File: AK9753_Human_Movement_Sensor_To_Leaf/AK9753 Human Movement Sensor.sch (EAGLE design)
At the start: 9 parts, among them J3 PTH, U2 AK9753

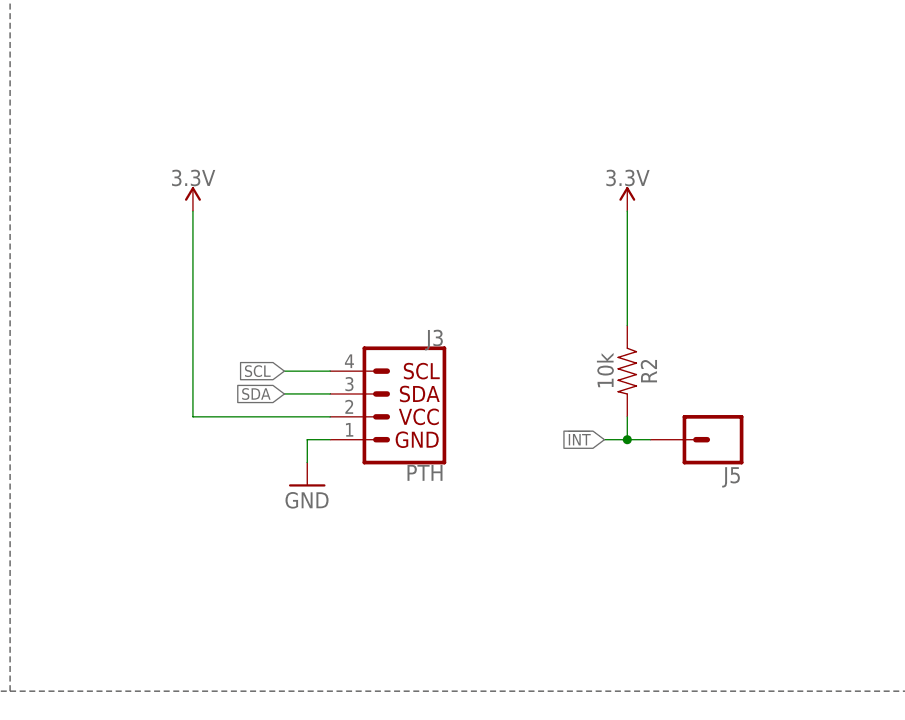
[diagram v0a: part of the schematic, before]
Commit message: Finished schematic
drawing board next
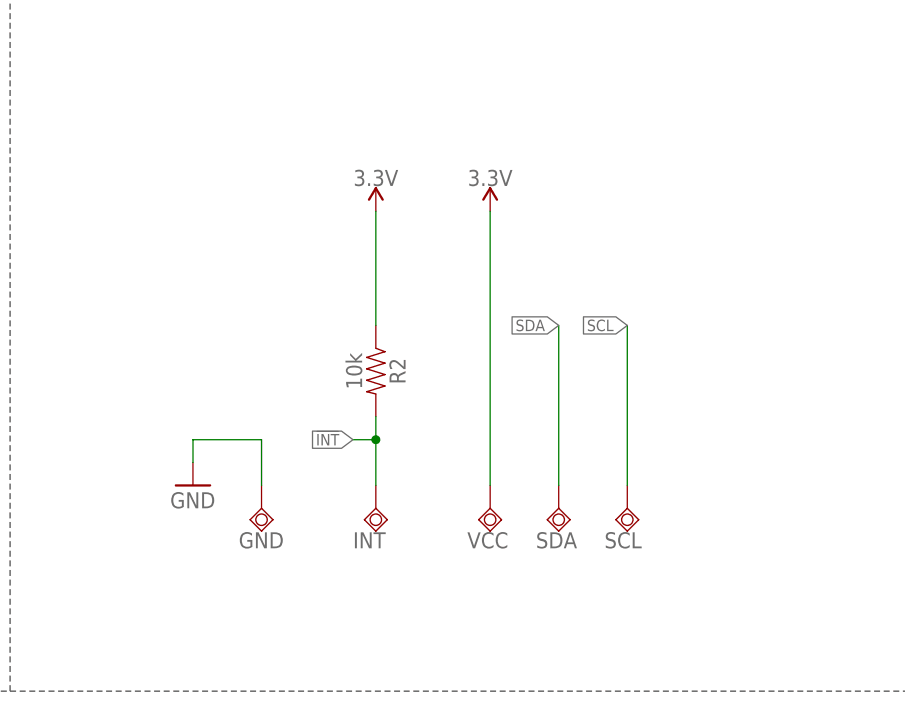
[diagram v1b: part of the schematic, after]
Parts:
- removed J3: PTH, SparkFun-Connectors:I2C_STANDARD_NO_SILK
- removed J5: (no value), SparkFun-Connectors:CONN_01PTH_NO_SILK_YES_STOP
- added GND, INT, SCL, SDA, VCC: TPSQTP20R, testpad:TPSQTP20R
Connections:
- net !INT: now also INT.TP; no longer J5.1
- net 3.3V: now also VCC.TP; no longer J3.2
- net GND: now also GND.TP; no longer J3.1
- net SCL: now also SCL.TP; no longer J3.4
- net SDA: now also SDA.TP; no longer J3.3
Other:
- moved on the sheet: R2
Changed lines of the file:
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@@
 <part name="GND4" library="SparkFun" deviceset="GND" device=""/>
 <part name="SUPPLY7" library="SparkFun-PowerSymbols" deviceset="3.3V" device=""/>
-<part name="J3" library="SparkFun-Connectors" deviceset="I2C_STANDARD" device="_NO_SILK" value="PTH"/>
 <part name="GND7" library="SparkFun" deviceset="GND" device=""/>
 <part name="C4" library="SparkFun-Capacitors" deviceset="1.0UF" device="-0603-16V-10%" value="1.0uF"/>
-<part name="J5" library="SparkFun-Connectors" deviceset="CONN_01" device="PTH_NO_SILK_YES_STOP"/>
 <part name="U2" library="SparkFun-Sensors" deviceset="AK9750" device="&quot;" value="AK9753"/>
 <part name="SUPPLY6" library="SparkFun-PowerSymbols" deviceset="3.3V" device=""/>
@@
 <part name="R6" library="SparkFun-Resistors" deviceset="330OHM" device="-0603-1/10W-1%" value="330"/>
 <part name="SUPPLY10" library="SparkFun-PowerSymbols" deviceset="3.3V" device=""/>
+<part name="SDA" library="testpad" library_urn="urn:adsk.eagle:library:385" deviceset="TPSQ" device="TP20R" package3d_urn="urn:adsk.eagle:package:27973/1"/>
+<part name="VCC" library="testpad" library_urn="urn:adsk.eagle:library:385" deviceset="TPSQ" device="TP20R" package3d_urn="urn:adsk.eagle:package:27973/1"/>
+<part name="SCL" library="testpad" library_urn="urn:adsk.eagle:library:385" deviceset="TPSQ" device="TP20R" package3d_urn="urn:adsk.eagle:package:27973/1"/>
+<part name="GND" library="testpad" library_urn="urn:adsk.eagle:library:385" deviceset="TPSQ" device="TP20R" package3d_urn="urn:adsk.eagle:package:27973/1"/>
+<part name="INT" library="testpad" library_urn="urn:adsk.eagle:library:385" deviceset="TPSQ" device="TP20R" package3d_urn="urn:adsk.eagle:package:27973/1"/>
 </parts>
 <sheets>
@@
 <attribute name="VALUE" x="60.96" y="101.6" size="1.778" layer="96"/>
 </instance>
-<instance part="SUPPLY7" gate="G$1" x="160.02" y="144.78" smashed="yes">
-<attribute name="VALUE" x="160.02" y="147.574" size="1.778" layer="96" align="bottom-center"/>
-</instance>
-<instance part="J3" gate="G$1" x="182.88" y="121.92" smashed="yes" rot="MR0">
-<attribute name="VALUE" x="187.96" y="116.586" size="1.778" layer="96" font="vector" rot="MR0" align="top-left"/>
-<attribute name="NAME" x="187.96" y="129.794" size="1.778" layer="95" font="vector" rot="MR0"/>
-</instance>
-<instance part="GND7" gate="1" x="172.72" y="114.3" smashed="yes">
-<attribute name="VALUE" x="170.18" y="111.76" size="1.778" layer="96"/>
+<instance part="SUPPLY7" gate="G$1" x="193.04" y="144.78" smashed="yes">
+<attribute name="VALUE" x="193.04" y="147.574" size="1.778" layer="96" align="bottom-center"/>
+</instance>
+<instance part="GND7" gate="1" x="160.02" y="114.3" smashed="yes">
+<attribute name="VALUE" x="157.48" y="111.76" size="1.778" layer="96"/>
 </instance>
 <instance part="C4" gate="G$1" x="63.5" y="114.3" smashed="yes">
@@
 <attribute name="VALUE" x="65.024" y="112.141" size="1.778" layer="96" font="vector"/>
 </instance>
-<instance part="J5" gate="G$1" x="218.44" y="119.38" smashed="yes" rot="R180">
-<attribute name="VALUE" x="220.98" y="124.206" size="1.778" layer="96" font="vector" rot="R180"/>
-<attribute name="NAME" x="220.98" y="116.332" size="1.778" layer="95" font="vector" rot="R180"/>
-</instance>
 <instance part="U2" gate="U1" x="88.9" y="116.84" smashed="yes">
 <attribute name="NAME" x="78.74" y="125.222" size="1.778" layer="95" font="vector"/>
@@
 <attribute name="VALUE" x="52.324" y="112.141" size="1.778" layer="96" font="vector"/>
 </instance>
-<instance part="R2" gate="G$1" x="208.28" y="127" smashed="yes" rot="R270">
-<attribute name="NAME" x="209.804" y="127" size="1.778" layer="95" font="vector" rot="R270" align="bottom-center"/>
-<attribute name="VALUE" x="206.756" y="127" size="1.778" layer="96" font="vector" rot="R270" align="top-center"/>
-</instance>
-<instance part="SUPPLY9" gate="G$1" x="208.28" y="144.78" smashed="yes">
-<attribute name="VALUE" x="208.28" y="147.574" size="1.778" layer="96" align="bottom-center"/>
+<instance part="R2" gate="G$1" x="180.34" y="127" smashed="yes" rot="R270">
+<attribute name="NAME" x="181.864" y="127" size="1.778" layer="95" font="vector" rot="R270" align="bottom-center"/>
+<attribute name="VALUE" x="178.816" y="127" size="1.778" layer="96" font="vector" rot="R270" align="top-center"/>
+</instance>
+<instance part="SUPPLY9" gate="G$1" x="180.34" y="144.78" smashed="yes">
+<attribute name="VALUE" x="180.34" y="147.574" size="1.778" layer="96" align="bottom-center"/>
 </instance>
 <instance part="R6" gate="G$1" x="63.5" y="132.08" smashed="yes" rot="R90">
@@
 <instance part="SUPPLY10" gate="G$1" x="63.5" y="139.7" smashed="yes">
 <attribute name="VALUE" x="63.5" y="142.494" size="1.778" layer="96" align="bottom-center"/>
+</instance>
+<instance part="SDA" gate="G$1" x="200.66" y="111.76" smashed="yes">
+<attribute name="NAME" x="198.12" y="107.315" size="1.778" layer="95"/>
+<attribute name="TP_SIGNAL_NAME" x="203.2" y="110.49" size="1.778" layer="97"/>
+</instance>
+<instance part="VCC" gate="G$1" x="193.04" y="111.76" smashed="yes">
+<attribute name="NAME" x="190.5" y="107.315" size="1.778" layer="95"/>
+<attribute name="TP_SIGNAL_NAME" x="195.58" y="110.49" size="1.778" layer="97"/>
+</instance>
+<instance part="SCL" gate="G$1" x="208.28" y="111.76" smashed="yes">
+<attribute name="NAME" x="205.74" y="107.315" size="1.778" layer="95"/>
+<attribute name="TP_SIGNAL_NAME" x="210.82" y="110.49" size="1.778" layer="97"/>
+</instance>
+<instance part="GND" gate="G$1" x="167.64" y="111.76" smashed="yes">
+<attribute name="NAME" x="165.1" y="107.315" size="1.778" layer="95"/>
+<attribute name="TP_SIGNAL_NAME" x="170.18" y="110.49" size="1.778" layer="97"/>
+</instance>
+<instance part="INT" gate="G$1" x="180.34" y="111.76" smashed="yes">
+<attribute name="NAME" x="177.8" y="107.315" size="1.778" layer="95"/>
+<attribute name="TP_SIGNAL_NAME" x="182.88" y="110.49" size="1.778" layer="97"/>
 </instance>
 </instances>
@@
 </segment>
 <segment>
-<pinref part="J3" gate="G$1" pin="2"/>
-<wire x1="175.26" y1="121.92" x2="160.02" y2="121.92" width="0.1524" layer="91"/>
-<wire x1="160.02" y1="121.92" x2="160.02" y2="144.78" width="0.1524" layer="91"/>
+<wire x1="193.04" y1="114.3" x2="193.04" y2="144.78" width="0.1524" layer="91"/>
 <pinref part="SUPPLY7" gate="G$1" pin="3.3V"/>
+<pinref part="VCC" gate="G$1" pin="TP"/>
 </segment>
 <segment>
@@
 <pinref part="SUPPLY9" gate="G$1" pin="3.3V"/>
 <pinref part="R2" gate="G$1" pin="1"/>
-<wire x1="208.28" y1="132.08" x2="208.28" y2="144.78" width="0.1524" layer="91"/>
+<wire x1="180.34" y1="132.08" x2="180.34" y2="144.78" width="0.1524" layer="91"/>
 </segment>
 <segment>
@@
 </segment>
 <segment>
-<pinref part="J3" gate="G$1" pin="1"/>
-<wire x1="175.26" y1="119.38" x2="172.72" y2="119.38" width="0.1524" layer="91"/>
-<wire x1="172.72" y1="119.38" x2="172.72" y2="116.84" width="0.1524" layer="91"/>
+<wire x1="160.02" y1="119.38" x2="160.02" y2="116.84" width="0.1524" layer="91"/>
 <pinref part="GND7" gate="1" pin="GND"/>
+<pinref part="GND" gate="G$1" pin="TP"/>
+<wire x1="160.02" y1="119.38" x2="167.64" y2="119.38" width="0.1524" layer="91"/>
+<wire x1="167.64" y1="119.38" x2="167.64" y2="114.3" width="0.1524" layer="91"/>
 </segment>
 <segment>
@@
 </segment>
 <segment>
-<pinref part="J3" gate="G$1" pin="4"/>
-<wire x1="175.26" y1="127" x2="170.18" y2="127" width="0.1524" layer="91"/>
-<label x="170.18" y="127" size="1.27" layer="95" rot="R180" xref="yes"/>
+<label x="208.28" y="132.08" size="1.27" layer="95" rot="R180" xref="yes"/>
+<pinref part="SCL" gate="G$1" pin="TP"/>
+<wire x1="208.28" y1="132.08" x2="208.28" y2="114.3" width="0.1524" layer="91"/>
 </segment>
 </net>
@@
 </segment>
 <segment>
-<pinref part="J3" gate="G$1" pin="3"/>
-<wire x1="175.26" y1="124.46" x2="170.18" y2="124.46" width="0.1524" layer="91"/>
-<label x="170.18" y="124.46" size="1.27" layer="95" rot="R180" xref="yes"/>
+<label x="200.66" y="132.08" size="1.27" layer="95" rot="R180" xref="yes"/>
+<pinref part="SDA" gate="G$1" pin="TP"/>
+<wire x1="200.66" y1="132.08" x2="200.66" y2="114.3" width="0.1524" layer="91"/>
 </segment>
 </net>
 <net name="!INT" class="0">
 <segment>
-<wire x1="210.82" y1="119.38" x2="208.28" y2="119.38" width="0.1524" layer="91"/>
-<label x="205.74" y="119.38" size="1.27" layer="95" rot="R180" xref="yes"/>
-<pinref part="J5" gate="G$1" pin="1"/>
+<label x="177.8" y="119.38" size="1.27" layer="95" rot="R180" xref="yes"/>
 <pinref part="R2" gate="G$1" pin="2"/>
-<wire x1="208.28" y1="119.38" x2="205.74" y2="119.38" width="0.1524" layer="91"/>
-<wire x1="208.28" y1="121.92" x2="208.28" y2="119.38" width="0.1524" layer="91"/>
-<junction x="208.28" y="119.38"/>
+<wire x1="180.34" y1="119.38" x2="177.8" y2="119.38" width="0.1524" layer="91"/>
+<wire x1="180.34" y1="121.92" x2="180.34" y2="119.38" width="0.1524" layer="91"/>
+<junction x="180.34" y="119.38"/>
+<pinref part="INT" gate="G$1" pin="TP"/>
+<wire x1="180.34" y1="114.3" x2="180.34" y2="119.38" width="0.1524" layer="91"/>
 </segment>
 <segment>
@@
 </schematic>
 </drawing>
+<compatibility>
+<note version="8.2" severity="warning">
+Since Version 8.2, EAGLE supports online libraries. The ids
+of those online libraries will not be understood (or retained)
+with this version.
+</note>
+<note version="8.3" severity="warning">
+Since Version 8.3, EAGLE supports URNs for individual library
+assets (packages, symbols, and devices). The URNs of those assets
+will not be understood (or retained) with this version.
+</note>
+<note version="8.3" severity="warning">
+Since Version 8.3, EAGLE supports the association of 3D packages
+with devices in libraries, schematics, and board files. Those 3D
+packages will not be understood (or retained) with this version.
+</note>
+</compatibility>
 </eagle>

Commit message: PDFs
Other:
- note added: "Design By Louise Lessél, 2020 Based on SparkFun Breakout board https://www.sparkfun.com/products/14349"
- note removed: "Louise Lessel"
- moved on the sheet: C1, C4, GND, INT, R2, R4, R5, R6, SCL, SDA, U2, VCC
